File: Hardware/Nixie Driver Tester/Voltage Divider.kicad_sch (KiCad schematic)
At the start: 2 parts

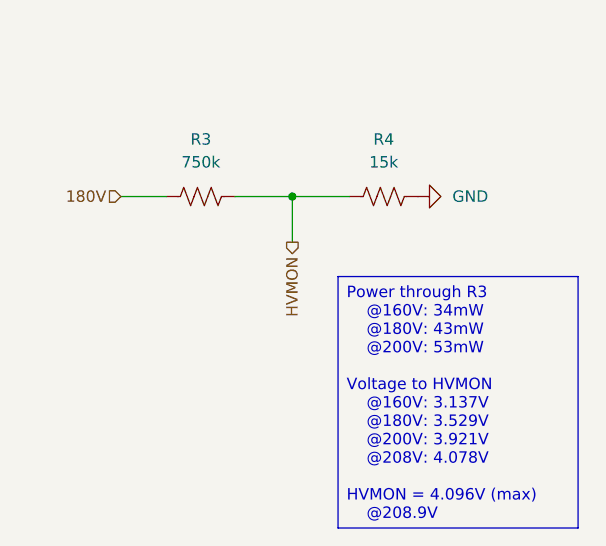
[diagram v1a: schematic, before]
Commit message: Switch mode 3.3V and SMD inductor
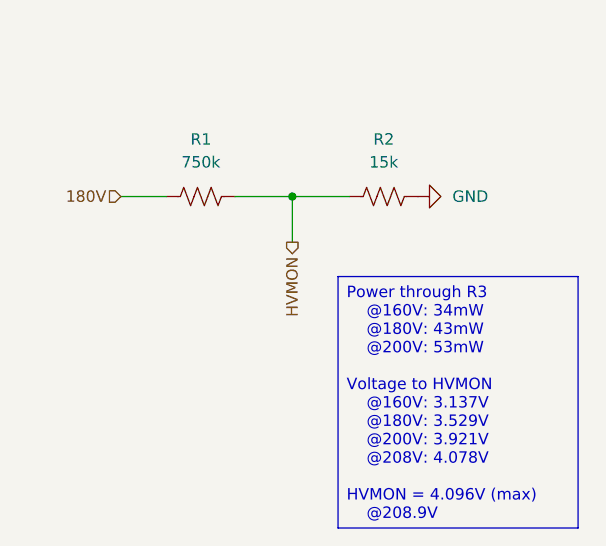
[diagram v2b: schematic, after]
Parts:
- renumbered R3 to R1, R4 to R2
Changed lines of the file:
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@@
 		(dnp no)
 		(fields_autoplaced yes)
-		(property "Reference" "R3"
+		(property "Reference" "R1"
 			(at 123.19 95.25 90)
 			(show_name no)
@@
 			(project "Nixie Driver Tester"
 				(path "/c2082ee6-4c2e-4b3c-b2d7-410eae192cfe/ae5fc040-94ea-4df2-9d60-7848f7e17a3f"
-					(reference "R3")
+					(reference "R1")
 					(unit 1)
 				)
@@
 		(dnp no)
 		(fields_autoplaced yes)
-		(property "Reference" "#PWR09"
+		(property "Reference" "#PWR08"
 			(at 153.67 101.6 0)
 			(hide yes)
@@
 			(project "Nixie Driver Tester"
 				(path "/c2082ee6-4c2e-4b3c-b2d7-410eae192cfe/ae5fc040-94ea-4df2-9d60-7848f7e17a3f"
-					(reference "#PWR09")
+					(reference "#PWR08")
 					(unit 1)
 				)
@@
 		(dnp no)
 		(fields_autoplaced yes)
-		(property "Reference" "R4"
+		(property "Reference" "R2"
 			(at 143.51 95.25 90)
 			(show_name no)
@@
 			(project "Nixie Driver Tester"
 				(path "/c2082ee6-4c2e-4b3c-b2d7-410eae192cfe/ae5fc040-94ea-4df2-9d60-7848f7e17a3f"
-					(reference "R4")
+					(reference "R2")
 					(unit 1)
 				)

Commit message: Added test points
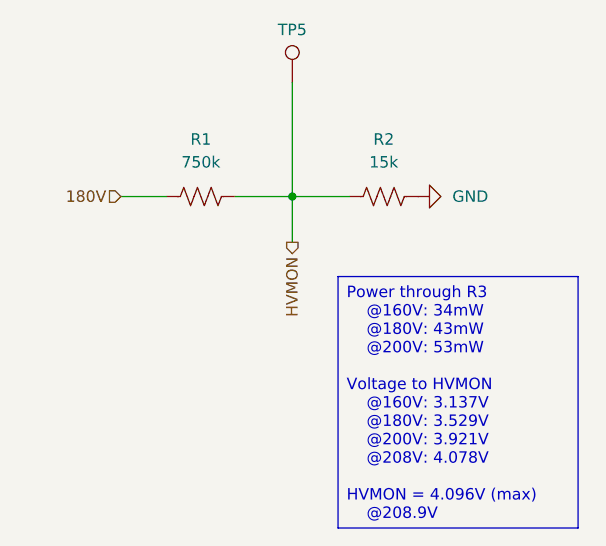
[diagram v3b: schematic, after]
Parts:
- added TP5: MON, TestPoint:TestPoint_Keystone_5015_Micro_Mini, symbol Connector:TestPoint
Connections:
- net HVMON: now also TP5.1
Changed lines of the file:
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@@
+	(wire
+		(pts
+			(xy 133.35 88.9) (xy 133.35 101.6)
+		)
+		(stroke
+			(width 0)
+			(type default)
+		)
+	)
 	(wire
 		(pts
@@
 		(dnp no)
 		(fields_autoplaced yes)
-		(property "Reference" "#PWR08"
+		(property "Reference" "#PWR09"
 			(at 153.67 101.6 0)
 			(hide yes)
@@
 			(project "Nixie Driver Tester"
 				(path "/c2082ee6-4c2e-4b3c-b2d7-410eae192cfe/ae5fc040-94ea-4df2-9d60-7848f7e17a3f"
-					(reference "#PWR08")
+					(reference "#PWR09")
 					(unit 1)
 				)
+			)
+		)
+	)
+	(symbol
+		(lib_id "Connector:TestPoint")
+		(at 133.35 88.9 0)
+		(unit 1)
+		(body_style 1)
+		(exclude_from_sim no)
+		(in_bom yes)
+		(on_board yes)
+		(in_pos_files yes)
+		(dnp no)
+		(property "Reference" "TP5"
+			(at 133.35 83.82 0)
+			(show_name no)
+			(do_not_autoplace no)
+			(effects
+				(font
+					(size 1.27 1.27)
+				)
+				(justify bottom)
+			)
+		)
+		(property "Value" "MON"
+			(at 135.89 86.8679 0)
+			(hide yes)
+			(show_name no)
+			(do_not_autoplace no)
+			(effects
+				(font
+					(size 1.27 1.27)
+				)
+				(justify left)
+			)
+		)
+		(property "Footprint" "TestPoint:TestPoint_Keystone_5015_Micro_Mini"
+			(at 138.43 88.9 0)
+			(hide yes)
+			(show_name no)
+			(do_not_autoplace no)
+			(effects
+				(font
+					(size 1.27 1.27)
+				)
+			)
+		)
+		(property "Datasheet" ""
+			(at 138.43 88.9 0)
+			(hide yes)
+			(show_name no)
+			(do_not_autoplace no)
+			(effects
+				(font
+					(size 1.27 1.27)
+				)
+			)
+		)
+		(property "Description" "test point"
+			(at 133.35 88.9 0)
+			(hide yes)
+			(show_name no)
+			(do_not_autoplace no)
+			(effects
+				(font
+					(size 1.27 1.27)
+				)
+			)
+		)
+		(pin "1"
+		)
+		(instances
+			(project "Nixie Driver Tester"
+				(path "/c2082ee6-4c2e-4b3c-b2d7-410eae192cfe/ae5fc040-94ea-4df2-9d60-7848f7e17a3f"
+					(reference "TP5")
+					(unit 1)
+				)

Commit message: new values for voltage divider
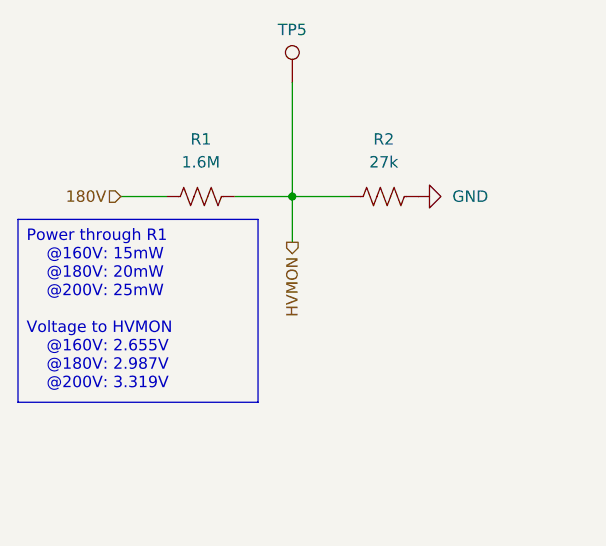
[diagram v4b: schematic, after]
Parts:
- R1: value 750k -> 1.6M
- R2: value 15k -> 27k
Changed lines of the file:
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@@
 	(generator_version "10.0")
 	(paper "A4")
-	(text_box "Power through R3\n	@160V: 34mW\n	@180V: 43mW\n	@200V: 53mW\n\nVoltage to HVMON\n	@160V: 3.137V\n	@180V: 3.529V\n	@200V: 3.921V\n	@208V: 4.078V\n\nHVMON = 4.096V (max)\n	@208.9V"
-		(exclude_from_sim no)
-		(at 138.43 110.49 0)
-		(size 26.67 27.94)
+	(text_box "Power through R1\n	@160V: 15mW\n	@180V: 20mW\n	@200V: 25mW\n\nVoltage to HVMON\n	@160V: 2.655V\n	@180V: 2.987V\n	@200V: 3.319V"
+		(exclude_from_sim no)
+		(at 102.87 104.14 0)
+		(size 26.67 20.32)
 		(margins 0.9525 0.9525 0.9525 0.9525)
 		(stroke
 			(width 0)
-			(type default)
+			(type solid)
 		)
 		(fill
@@
 			)
 		)
-		(property "Value" "750k"
+		(property "Value" "1.6M"
 			(at 123.19 97.79 90)
 			(show_name no)
@@
 			)
 		)
-		(property "Value" "15k"
+		(property "Value" "27k"
 			(at 143.51 97.79 90)
 			(show_name no)
